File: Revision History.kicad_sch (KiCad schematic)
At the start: 0 parts

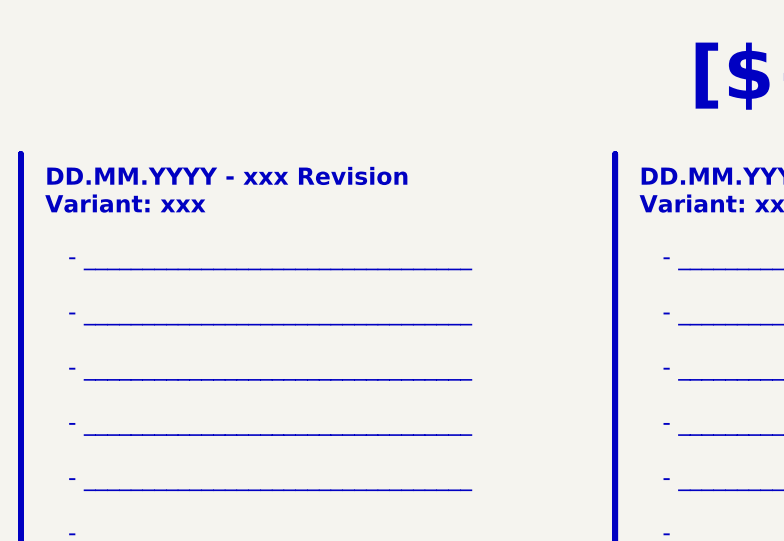
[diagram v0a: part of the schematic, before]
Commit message: Progress in power input and sata power option
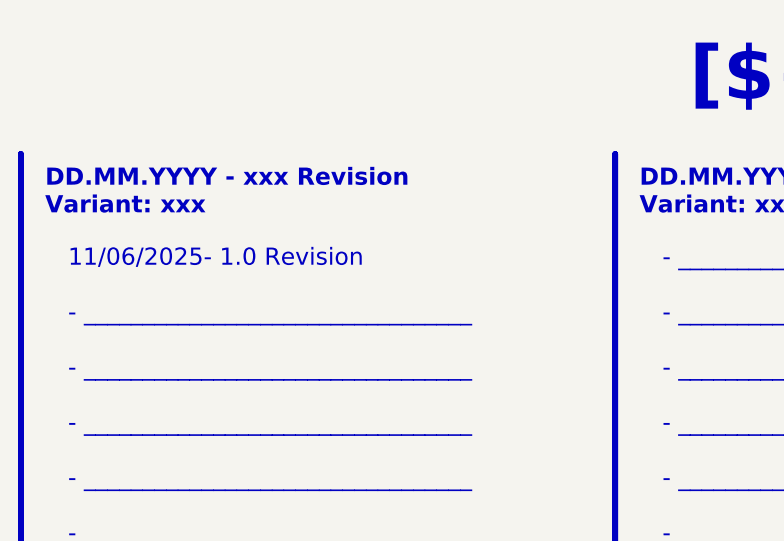
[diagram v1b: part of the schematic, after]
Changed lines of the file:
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@@
 		)
 	)
-	(text_box "- _________________________________\n\n- _________________________________\n\n- _________________________________\n\n- _________________________________\n\n- _________________________________\n\n- _________________________________\n\n- _________________________________\n\n- _________________________________\n\n- _________________________________\n\n- _________________________________\n\n- _________________________________\n\n- _________________________________\n\n- _________________________________\n\n- _________________________________\n\n- _________________________________\n\n- _________________________________\n\n- _________________________________"
+	(text_box "11/06/2025- 1.0 Revision\n\n- _________________________________\n\n- _________________________________\n\n- _________________________________\n\n- _________________________________\n\n- _________________________________\n\n- _________________________________\n\n- _________________________________\n\n- _________________________________\n\n- _________________________________\n\n- _________________________________\n\n- _________________________________\n\n- _________________________________\n\n- _________________________________\n\n- _________________________________\n\n- _________________________________\n\n- _________________________________"
 		(exclude_from_sim no)
 		(at 22.86 40.64 0)
@@
 		(stroke
 			(width -0.0001)
-			(type default)
+			(type solid)
 		)
 		(fill
